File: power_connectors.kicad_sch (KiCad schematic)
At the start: 7 parts, among them CN1 4P JST VH

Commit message: commit before updating to LiveAstra lib
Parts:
- removed TP16, TP17: TestPoint_Thimble, TestPoint:TestPoint_Loop_D3.50mm_Drill0.9mm_Beaded, symbol EASYEDA2KICAD:TestPoint_Thimble

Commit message: Updated library name, updated and verified all footprints
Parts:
- CN1: footprint EASYEDA2KICAD:JST_VH_B4P-VH-B_1x04_P3.96mm_Vertical -> LiveAstra:JST_VH_B4P-VH-B_1x04_P3.96mm_Vertical; symbol EASYEDA2KICAD:JST_VH_4PIN_10A_250V -> LiveAstra:JST_VH_4PIN_10A_250V
- D2, D3: footprint EASYEDA2KICAD:SMB_L4.6-W3.6-LS5.3-BI -> LiveAstra:SMB_L4.6-W3.6-LS5.3-BI; symbol EASYEDA2KICAD:D_TVS_BIDI_600W -> LiveAstra:D_TVS_BIDI_600W
- TP18, TP19: symbol EASYEDA2KICAD:TestPoint_Thimble -> LiveAstra:TestPoint_Thimble
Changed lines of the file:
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@@
 	)
 	(symbol
-		(lib_id "EASYEDA2KICAD:CHASSIS")
+		(lib_id "LiveAstra:CHASSIS")
 		(at 152.4 100.33 0)
 		(unit 1)
@@
 	)
 	(symbol
-		(lib_id "EASYEDA2KICAD:TestPoint_Thimble")
+		(lib_id "LiveAstra:TestPoint_Thimble")
 		(at 203.2 101.6 0)
 		(unit 1)
@@
 	)
 	(symbol
-		(lib_id "EASYEDA2KICAD:D_TVS_BIDI_600W")
+		(lib_id "LiveAstra:D_TVS_BIDI_600W")
 		(at 101.6 93.98 90)
 		(unit 1)
@@
 			)
 		)
-		(property "Footprint" "EASYEDA2KICAD:SMB_L4.6-W3.6-LS5.3-BI"
+		(property "Footprint" "LiveAstra:SMB_L4.6-W3.6-LS5.3-BI"
 			(at 110.49 93.98 0)
 			(effects
@@
 	)
 	(symbol
-		(lib_id "EASYEDA2KICAD:CHASSIS")
+		(lib_id "LiveAstra:CHASSIS")
 		(at 101.6 100.33 0)
 		(unit 1)
@@
 	)
 	(symbol
-		(lib_id "EASYEDA2KICAD:JST_VH_4PIN_10A_250V")
+		(lib_id "LiveAstra:JST_VH_4PIN_10A_250V")
 		(at 71.12 83.82 180)
 		(unit 1)
@@
 			)
 		)
-		(property "Footprint" "EASYEDA2KICAD:JST_VH_B4P-VH-B_1x04_P3.96mm_Vertical"
+		(property "Footprint" "LiveAstra:JST_VH_B4P-VH-B_1x04_P3.96mm_Vertical"
 			(at 71.12 63.5 0)
 			(effects
@@
 	)
 	(symbol
-		(lib_id "EASYEDA2KICAD:CHASSIS")
+		(lib_id "LiveAstra:CHASSIS")
 		(at 203.2 81.28 0)
 		(unit 1)
@@
 	)
 	(symbol
-		(lib_id "EASYEDA2KICAD:CHASSIS")
+		(lib_id "LiveAstra:CHASSIS")
 		(at 228.6 104.14 0)
 		(unit 1)
@@
 	)
 	(symbol
-		(lib_id "EASYEDA2KICAD:D_TVS_BIDI_600W")
+		(lib_id "LiveAstra:D_TVS_BIDI_600W")
 		(at 152.4 93.98 90)
 		(unit 1)
@@
 			)
 		)
-		(property "Footprint" "EASYEDA2KICAD:SMB_L4.6-W3.6-LS5.3-BI"
+		(property "Footprint" "LiveAstra:SMB_L4.6-W3.6-LS5.3-BI"
 			(at 161.29 93.98 0)
 			(effects
@@
 	)
 	(symbol
-		(lib_id "EASYEDA2KICAD:TestPoint_Thimble")
+		(lib_id "LiveAstra:TestPoint_Thimble")
 		(at 228.6 101.6 0)
 		(unit 1)

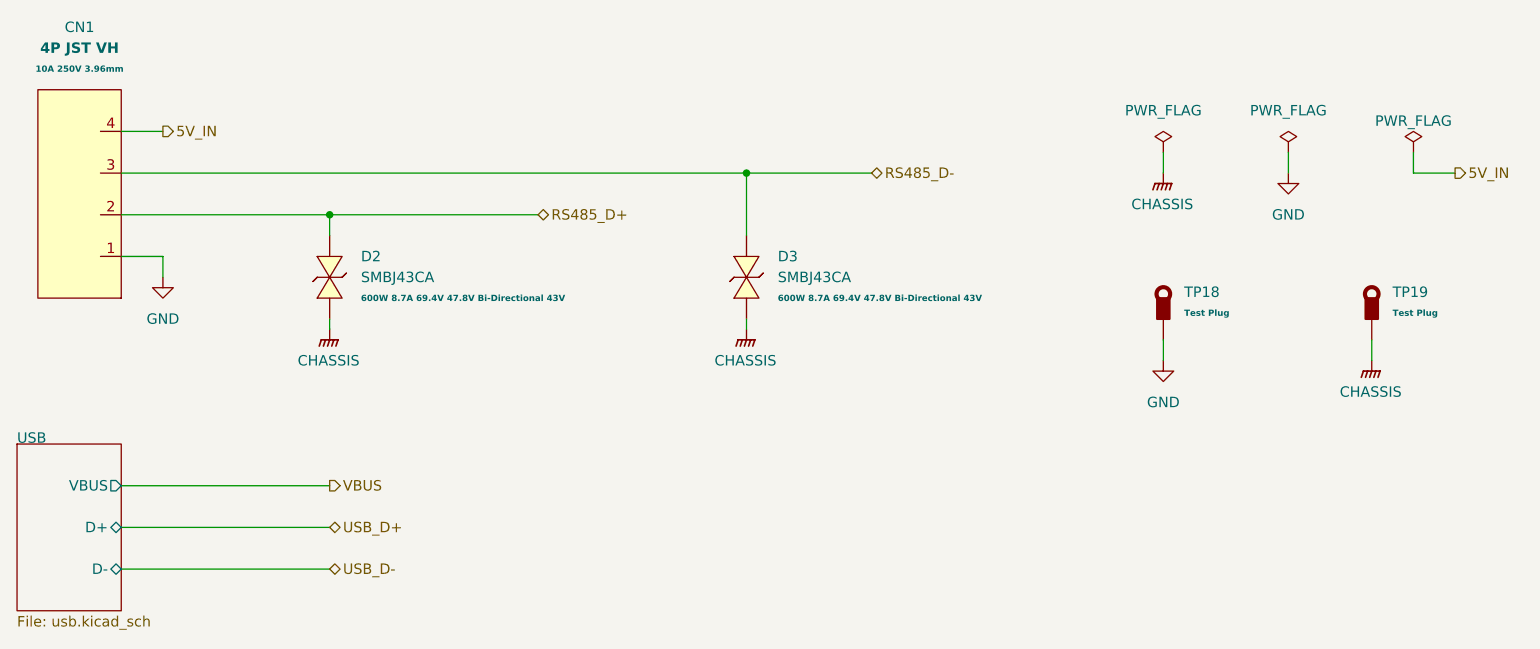
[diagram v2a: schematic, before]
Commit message: Finished layout no drc or erc errors
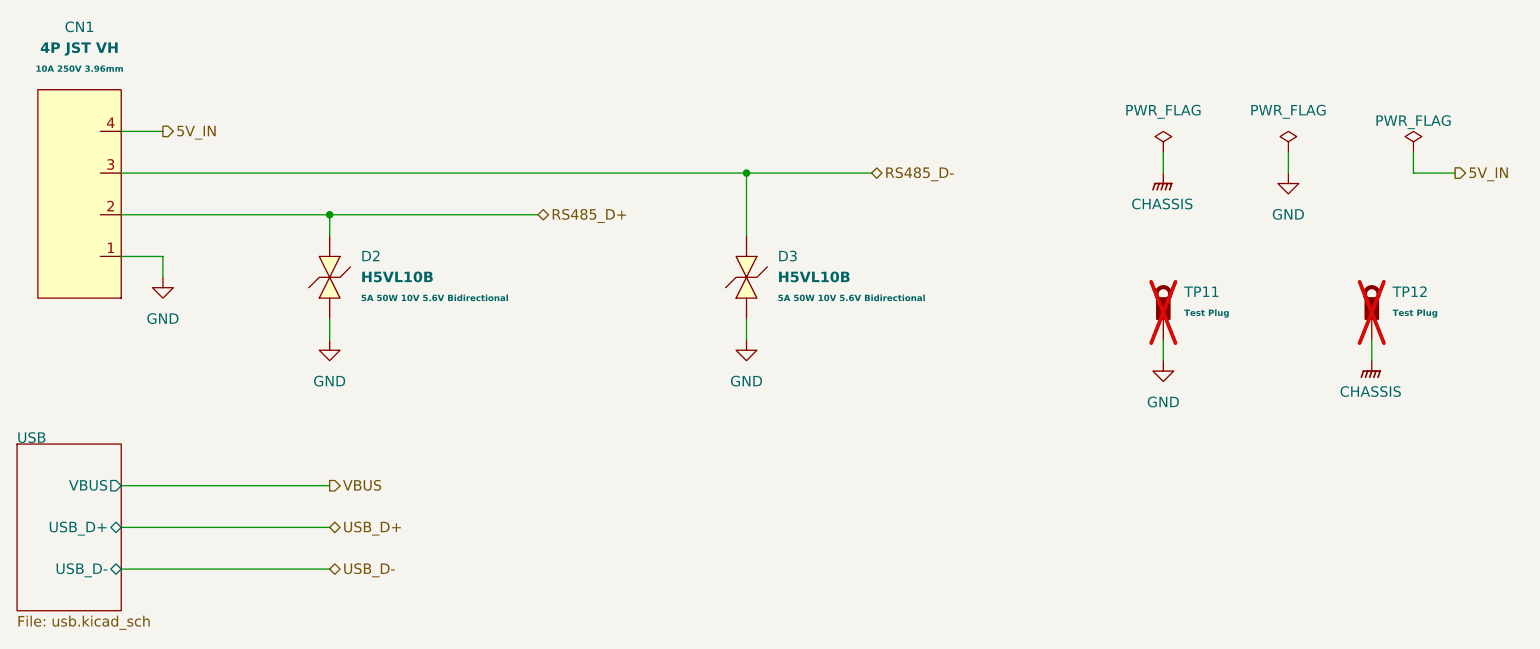
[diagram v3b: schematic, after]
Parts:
- removed D2, D3: SMBJ43CA, LiveAstra:SMB_L4.6-W3.6-LS5.3-BI, symbol LiveAstra:D_TVS_BIDI_600W
- added D2, D3: H5VL10B, LiveAstra:D_DFN0603_H5VL10B_Bidirectional_TVS, symbol LiveAstra:D_TVS_H5VL10B_BIDI_50W
- TP11: renamed from TP18; footprint TestPoint:TestPoint_Loop_D3.50mm_Drill0.9mm_Beaded -> LiveAstra:TestPoint_Loop_D3.50mm_Drill0.9mm_Beaded; now not fitted; now left out of the parts list
- TP12: renamed from TP19; footprint TestPoint:TestPoint_Loop_D3.50mm_Drill0.9mm_Beaded -> LiveAstra:TestPoint_Loop_D3.50mm_Drill0.9mm_Beaded; now not fitted; now left out of the parts list
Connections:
- net GND: now also D2.1 (C), D3.1 (C)
- net RS485_D+: now also D2.2 (A)
- net RS485_D-: now also D3.2 (A)
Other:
- sheet USB ports: added USB_D+, USB_D-; removed D+, D-

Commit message: workflow
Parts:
- TP11, TP12: now fitted
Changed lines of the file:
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@@
+			)
+		)
+		(property "Extra Value" ""
+			(at 101.6 93.98 0)
+			(effects
+				(font
+					(size 1.27 1.27)
+				)
+				(hide yes)
 			)
 		)
@@
 			)
 		)
+		(property "Extra Value" ""
+			(at 152.4 93.98 0)
+			(effects
+				(font
+					(size 1.27 1.27)
+				)
+				(hide yes)
+			)
+		)
 		(pin "1"
 		)
@@
 		(in_bom no)
 		(on_board yes)
-		(dnp yes)
+		(dnp no)
 		(fields_autoplaced yes)
 		(property "Reference" "TP11"
@@
 			)
 		)
+		(property "Extra Value" ""
+			(at 203.2 101.6 0)
+			(effects
+				(font
+					(size 1.27 1.27)
+				)
+				(hide yes)
+			)
+		)
 		(pin "1"
 		)
@@
 			)
 		)
+		(property "Extra Value" ""
+			(at 71.12 83.82 0)
+			(effects
+				(font
+					(size 1.27 1.27)
+				)
+				(hide yes)
+			)
+		)
 		(pin "1"
 		)
@@
 		(in_bom no)
 		(on_board yes)
-		(dnp yes)
+		(dnp no)
 		(fields_autoplaced yes)
 		(property "Reference" "TP12"
@@
 			)
 		)
+		(property "Extra Value" ""
+			(at 228.6 101.6 0)
+			(effects
+				(font
+					(size 1.27 1.27)
+				)
+				(hide yes)
+			)
+		)

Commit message: workflow
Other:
- title: (none) -> Power Connectors
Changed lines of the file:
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@@
 	(generator_version "8.0")
 	(paper "A4")
+	(title_block
+		(title "Power Connectors")
+	)
 	(junction
 		(at 101.6 86.36)
@@
 			(project "AstraControl"
 				(path "/9a751838-dce8-4d69-8a02-736625ac74e7/0db21d8e-3390-4d67-877f-0e5d98e37848/e0a60313-5e73-4a17-9374-b4b4ea2344cd"
-					(page "10")
-				)
-			)
+					(page "9")
+				)
+			)
